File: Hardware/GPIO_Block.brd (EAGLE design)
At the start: 30.5 x 71.1 mm, 14 parts, among them U2 EDISON_CONNECTOR_FULLMOUNTING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, U3 EDISON_CONNECTOR_FULLHEADER

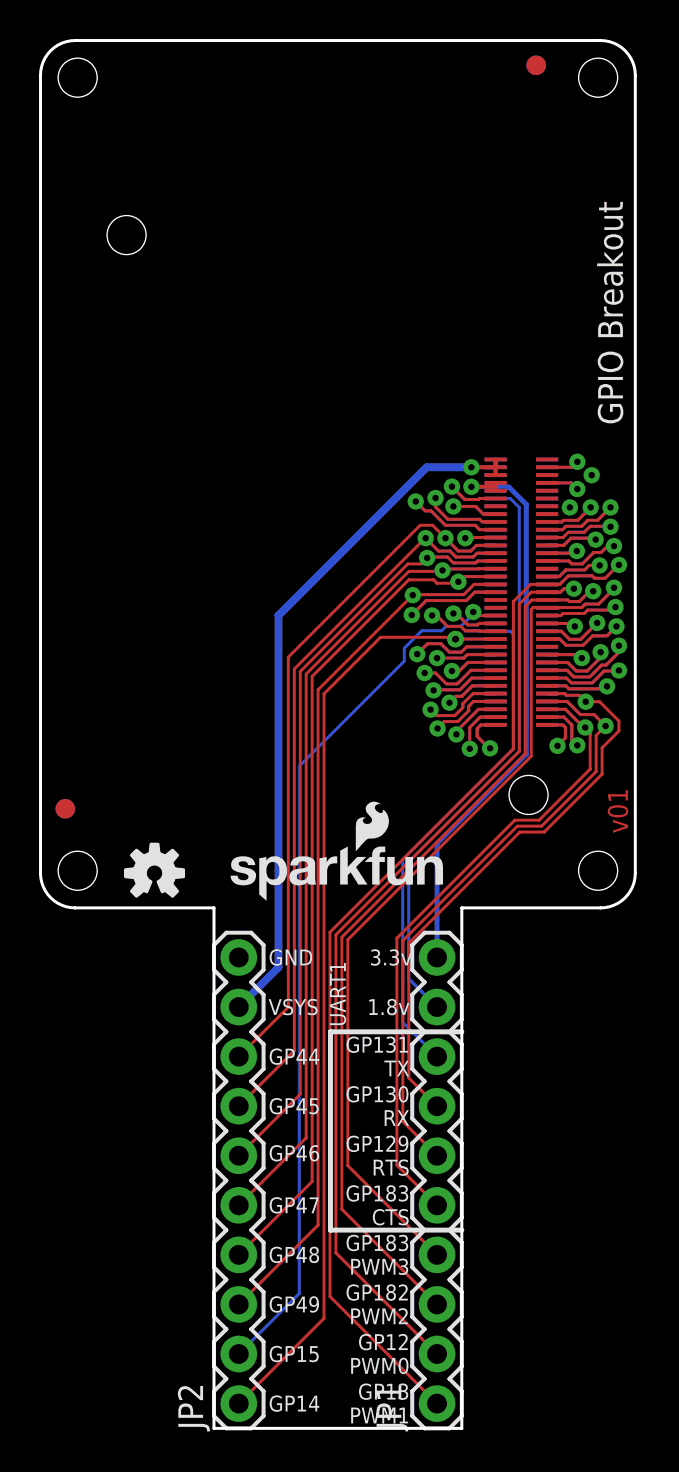
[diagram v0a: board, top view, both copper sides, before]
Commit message: added level shifters with the ability to select from vsys and 3.3v cleaned up copper pours changed name on board and files added DCIN pin cleaned up units of board.
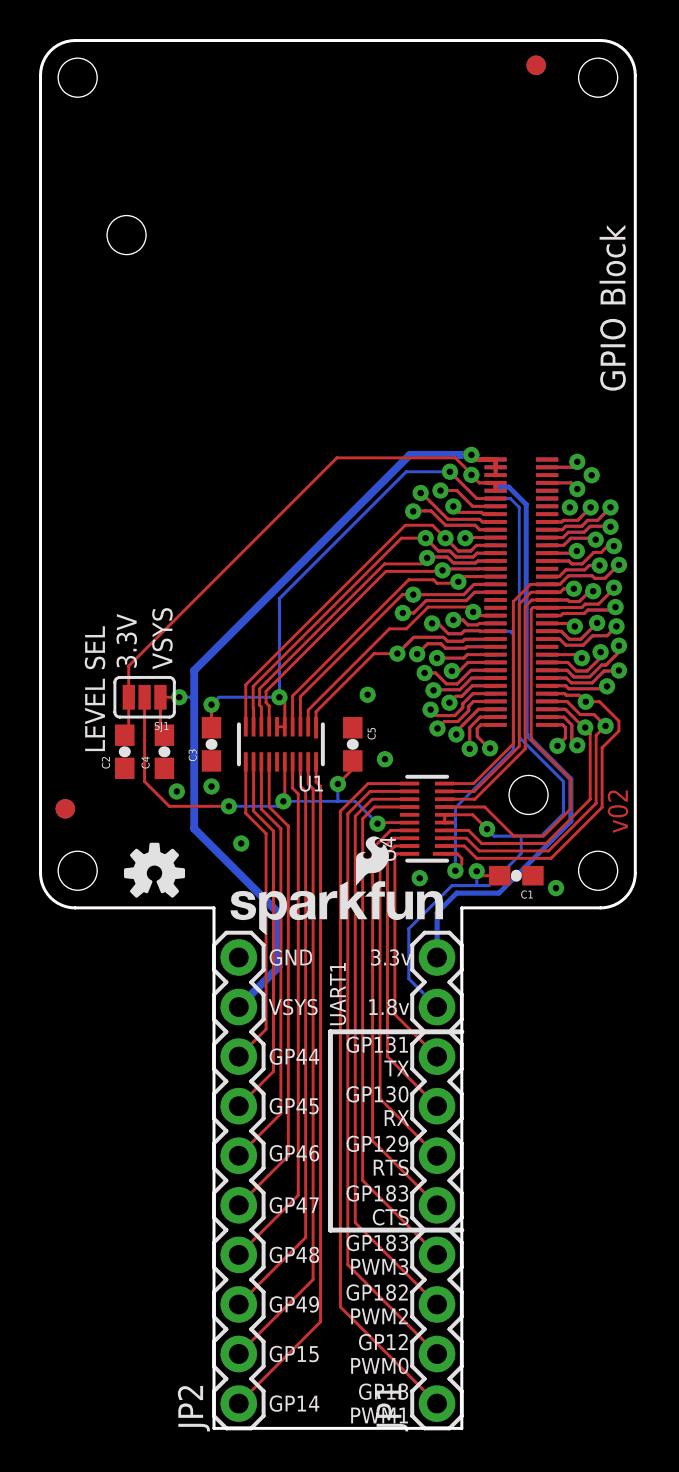
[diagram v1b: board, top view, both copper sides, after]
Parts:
- added C1, C2, C3, C4, C5: 0.1uF, SparkFun-Capacitors:0603-CAP
- added SJ1: GPIO Reference Select, SparkFun-Passives:PAD-JUMPER-3-2OF3_NC_BY_PASTE_YES_SILK_FULL_BOX
- added U1, U4: TXB0108, Testing:UFDFN-20
- moved LOGO3 1.78 mm to (21.2, -1.52)
- moved LOGO4 1.78 mm to (9.30, -1.52)
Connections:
- new net DCIN: U2.14, U3.14
- new net GPIO_REFERENCE_SELECT: C5.2, SJ1.2, U1.16, U4.16
- new net N$1: JP2.8, U1.11
- new net N$11: JP1.4, U4.14
- new net N$12: JP1.3, U4.13
- new net N$13: JP1.2, U4.12
- new net N$14: JP1.1, U4.11
- new net N$15: JP1.5, U4.17
- new net N$16: JP1.6, U4.18
- new net N$17: JP1.7, U4.19
- new net N$18: JP1.8, U4.20
- new net N$2: JP2.7, U1.12
- new net N$3: JP2.6, U1.13
- new net N$4: JP2.5, U1.14
- new net N$5: JP2.4, U1.17
- new net N$6: JP2.3, U1.18
- new net N$7: JP2.2, U1.19
- new net N$8: JP2.1, U1.20
- net 1.8V: now also C1.2, C3.2, U1.5, U1.6, U4.5, U4.6
- net 3.3V: now also C2.2, SJ1.3
- net GND: now also C1.1, C2.1, C3.1, C4.1, C5.1, U1.15, U4.15
- net GP128_UART_1_CTS: now also U4.4; no longer JP1.5
- net GP129_UART_1_RTS: now also U4.3; no longer JP1.6
- net GP12_PWM0: now also U4.9; no longer JP1.2
- net GP130_UART_1_RX: now also U4.2; no longer JP1.7
- net GP131_UART_1_TX: now also U4.1; no longer JP1.8
- net GP13_PWM1: now also U4.10; no longer JP1.1
- net GP14: now also U1.1; no longer JP2.1
- net GP15: now also U1.2; no longer JP2.2
- net GP182_PWM2: now also U4.8; no longer JP1.3
- net GP183_PWM3: now also U4.7; no longer JP1.4
- net GP44: now also U1.10; no longer JP2.8
- net GP45: now also U1.9; no longer JP2.7
- net GP46: now also U1.8; no longer JP2.6
- net GP47: now also U1.7; no longer JP2.5
- net GP48: now also U1.4; no longer JP2.4
- net GP49: now also U1.3; no longer JP2.3
- net VSYS: now also C4.2, SJ1.1
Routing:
- net N$14: track 0.00 -> 36.5 mm
- net GP13_PWM1: track 57.8 -> 22.1 mm
- net N$8: track 0.00 -> 34.7 mm
- net 1.8V: track 35.0 -> 69.5 mm, vias 1 -> 5
- net N$13: track 0.00 -> 33.2 mm
- net GP14: track 50.3 -> 17.2 mm, vias 2 -> 1
- net GP15: track 46.5 -> 14.0 mm
- net GP12_PWM0: track 49.0 -> 16.6 mm
- net N$7: track 0.00 -> 32.0 mm
- net GP49: track 49.0 -> 18.4 mm
- net N$12: track 0.00 -> 29.9 mm
- net 3.3V: track 30.9 -> 60.3 mm
- net N$6: track 0.00 -> 29.3 mm
- net GP182_PWM2: track 48.2 -> 19.0 mm
- net GP48: track 44.9 -> 16.7 mm
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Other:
- board text added: "3.3V"
- board text added: "GPIO Block"
- board text added: "LEVEL SEL"
- board text added: "NOTE: Units are in Inches"
- board text added: "v02"
- board text removed: "Connectors Go Here"
- board text removed: "GPIO Breakout"
- board text removed: "LED's and selector switches go here"
- board text removed: "Max Board Length"
- board text removed: "Nothing goes here... I mean it."
- board text removed: "v01"
